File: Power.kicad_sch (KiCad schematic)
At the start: 1 part

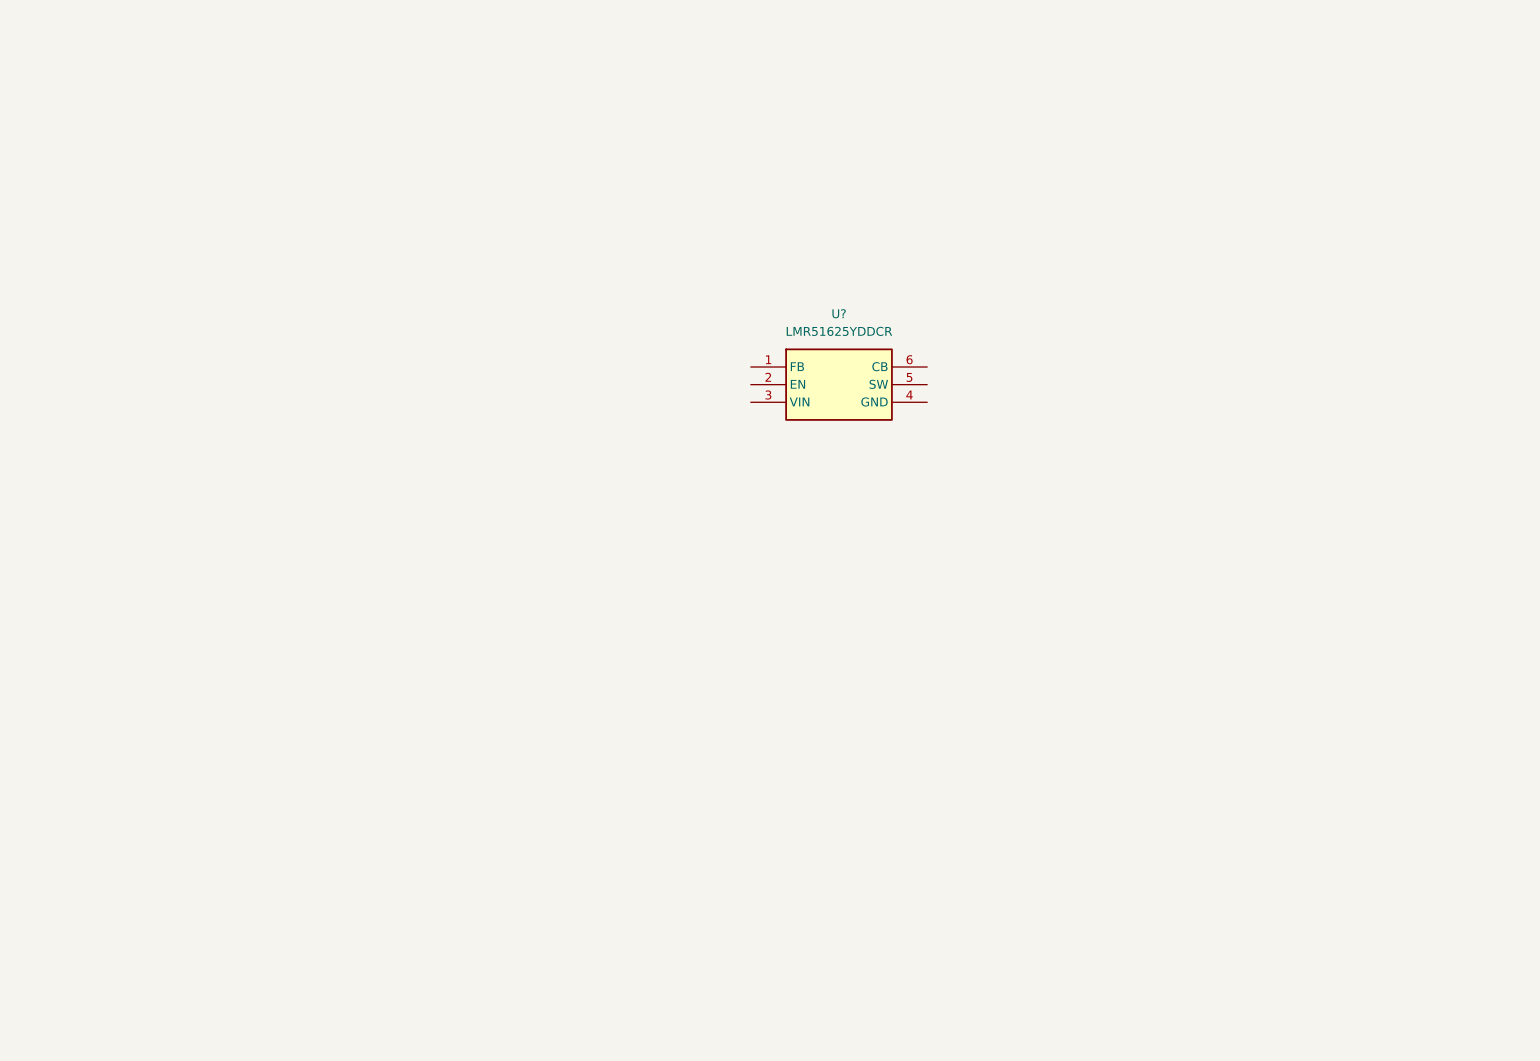
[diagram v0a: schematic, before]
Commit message: add power, some mcu components
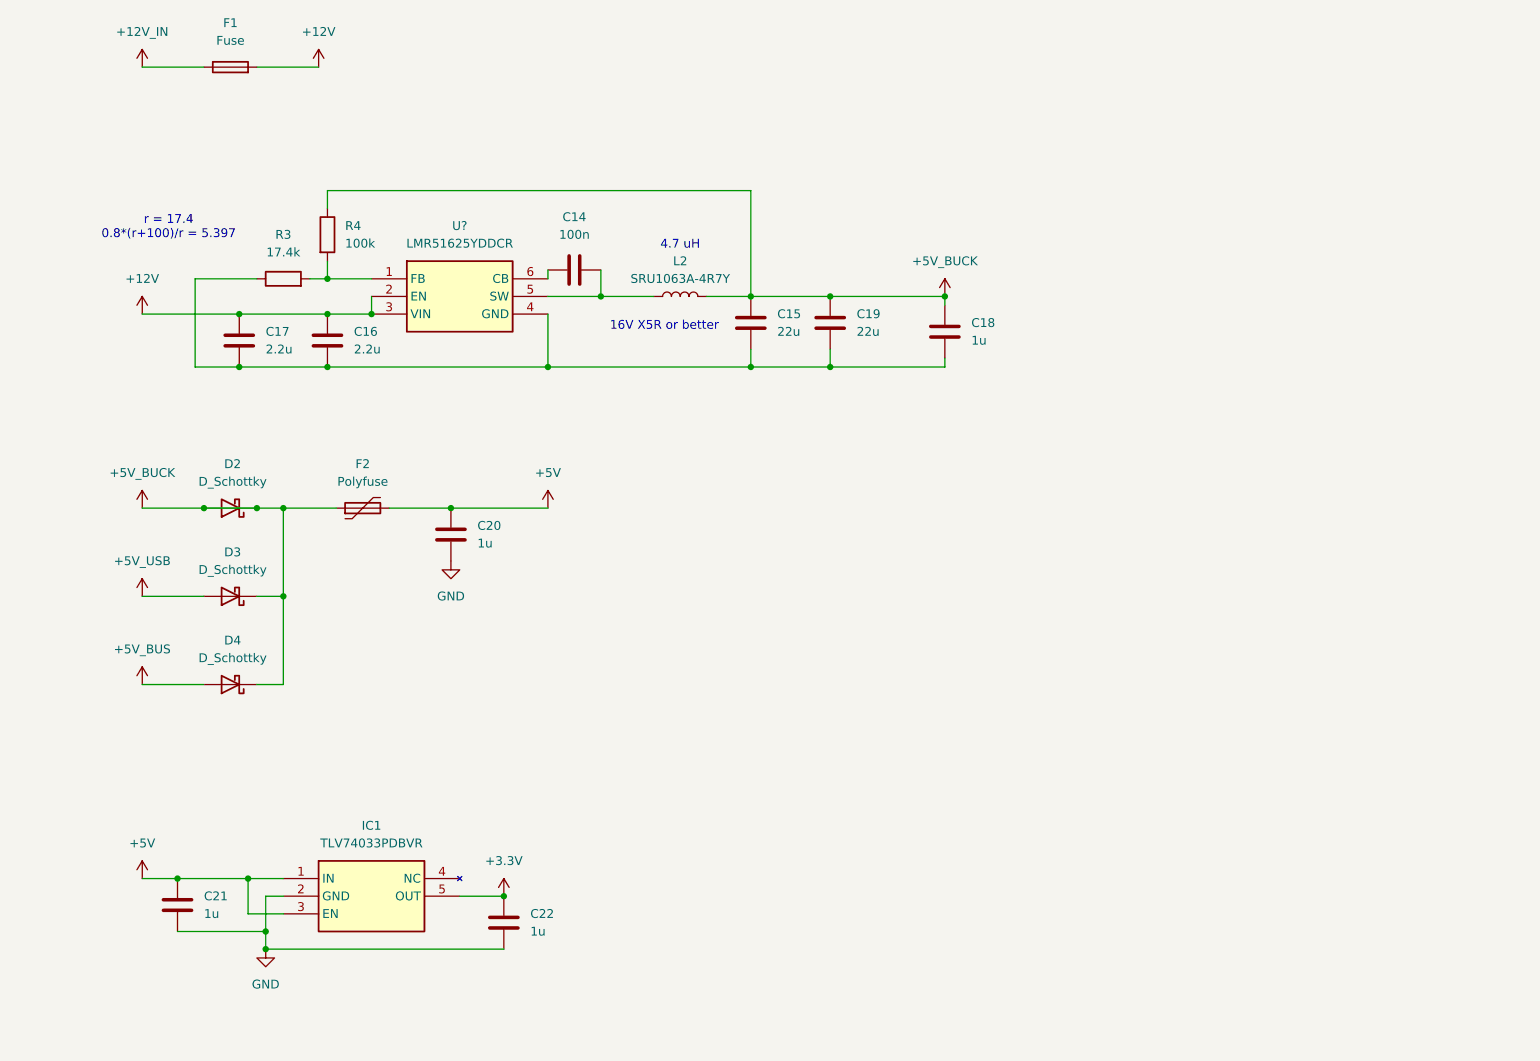
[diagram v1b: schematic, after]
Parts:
- added C14: 100n, Capacitor_SMD:C_0603_1608Metric_Pad1.08x0.95mm_HandSolder, symbol Device:C
- added C15, C19: 22u, Capacitor_SMD:C_1206_3216Metric_Pad1.33x1.80mm_HandSolder, symbol Device:C
- added C16, C17: 2.2u, Capacitor_SMD:C_0603_1608Metric_Pad1.08x0.95mm_HandSolder, symbol Device:C
- added C18, C20, C21, C22: 1u, Capacitor_SMD:C_0603_1608Metric_Pad1.08x0.95mm_HandSolder, symbol Device:C
- added D2, D3, D4: D_Schottky, Diode_SMD:D_SMA_Handsoldering, symbol Device:D_Schottky
- added F1: Fuse, Fuse:Fuseholder_Blade_Mini_Keystone_3568, symbol Device:Fuse
- added F2: Polyfuse, Fuse:Fuse_1812_4532Metric_Pad1.30x3.40mm_HandSolder, symbol Device:Polyfuse
- added IC1: TLV74033PDBVR, SamacSys_Parts:SOT95P280X145-5N, symbol SamacSys_Parts:TLV74033PDBVR
- added L2: SRU1063A-4R7Y, Inductor_SMD:L_Bourns-SRU1028_10.0x10.0mm, symbol Device:L
- added R3: 17.4k, Resistor_SMD:R_0603_1608Metric_Pad0.98x0.95mm_HandSolder, symbol Device:R
- added R4: 100k, Resistor_SMD:R_0603_1608Metric_Pad0.98x0.95mm_HandSolder, symbol Device:R
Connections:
- net at U?.1 (FB): now also R3.2, R4.2
- net +12V: now reaches U?.2 (EN)
- net +12V: now also U?.3 (VIN), C16.1, C17.1, F1.2
- net at U?.4 (GND): now also C15.2, C16.2, C17.2, C18.2, C19.2, R3.1
- net at U?.5 (SW): now also C14.2, L2.1
- net at U?.6 (CB): now also C14.1
- new net +12V_IN: F1.1
- new net +3.3V: C22.1, IC1.5 (OUT)
- new net +5V: C20.1, C21.1, F2.2, IC1.1 (IN), IC1.3 (EN)
- new net +5V_BUCK: C15.1, C18.1, C19.1, D2.1 (K), D2.2 (A), D3.1 (K), D4.1 (K), F2.1, L2.2, R4.1
- new net +5V_BUS: D4.2 (A)
- new net +5V_USB: D3.2 (A)
- new net GND: C20.2, C21.2, C22.2, IC1.2 (GND)
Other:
- note added: "16V X5R or better"
- note added: "4.7 uH"
- note added: "r = 17.4 0.8*(r+100)/r = 5.397"
- moved on the sheet: U?

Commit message: complete schematic, initial board layout
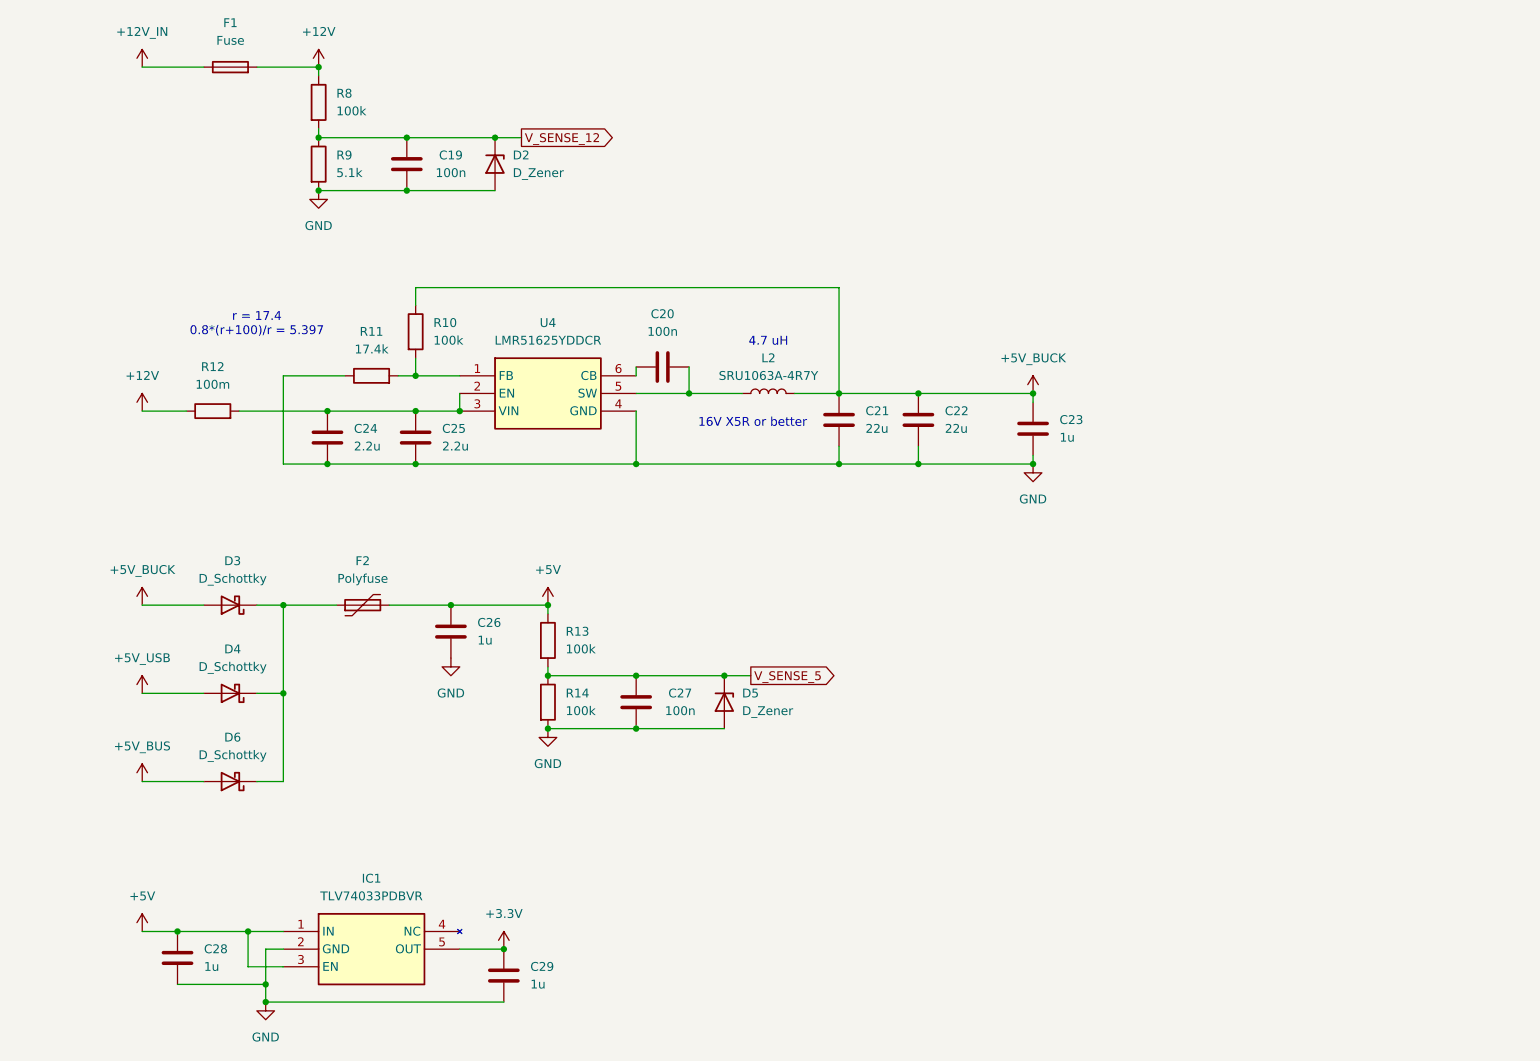
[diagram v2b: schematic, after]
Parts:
- added C19, C27: 100n, Capacitor_SMD:C_0603_1608Metric_Pad1.08x0.95mm_HandSolder, symbol Device:C
- added D2, D5: D_Zener, Diode_SMD:D_SOD-323, symbol Device:D_Zener
- added R12: 100m, Resistor_SMD:R_1206_3216Metric_Pad1.30x1.75mm_HandSolder, symbol Device:R
- added R13, R14, R8: 100k, Resistor_SMD:R_0603_1608Metric_Pad0.98x0.95mm_HandSolder, symbol Device:R
- added R9: 5.1k, Resistor_SMD:R_0603_1608Metric_Pad0.98x0.95mm_HandSolder, symbol Device:R
- D3: renamed from D2; footprint Diode_SMD:D_SMA_Handsoldering -> Diode_SMD:D_SMA
- D4: renamed from D3; footprint Diode_SMD:D_SMA_Handsoldering -> Diode_SMD:D_SMA
- D6: renamed from D4; footprint Diode_SMD:D_SMA_Handsoldering -> Diode_SMD:D_SMA
- gave numbers to parts that had none: 1
- renumbered C14 to C20, C15 to C21, C19 to C22, C18 to C23, C17 to C24, C16 to C25, C20 to C26, C21 to C28, C22 to C29, R4 to R10, R3 to R11
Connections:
- net +12V: now also R12.1, R8.1; no longer C24.1, C25.1, U4.2 (EN), U4.3 (VIN)
- net +5V: now also R13.1
- net +5V_BUCK: no longer D3.1 (K), D4.1 (K), D6.1 (K), F2.1
- net GND: now also C21.2, C22.2, C23.2, C24.2, C25.2, R11.1, U4.4 (GND), C19.2, C27.2, D2.2 (A), D5.2 (A), R14.2, R9.2
- new net: C24.1, C25.1, R12.2, U4.2 (EN), U4.3 (VIN)
- new net: D3.1 (K), D4.1 (K), D6.1 (K), F2.1
- new net V_SENSE_12: C19.1, D2.1 (K), R8.2, R9.1
- new net V_SENSE_5: C27.1, D5.1 (K), R13.2, R14.1
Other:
- moved on the sheet: C20, C21, C22, C23, C24, C25, C26, C28, C29, D3, D4, D6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

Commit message: layout almost complete
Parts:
- D2, D5: footprint Diode_SMD:D_SOD-323 -> Diode_SMD:D_SOD-323_HandSoldering
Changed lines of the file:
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@@
 			)
 		)
-		(property "Footprint" "Diode_SMD:D_SOD-323"
+		(property "Footprint" "Diode_SMD:D_SOD-323_HandSoldering"
 			(at 121.92 124.46 0)
 			(effects
@@
 			)
 		)
-		(property "Footprint" "Diode_SMD:D_SOD-323"
+		(property "Footprint" "Diode_SMD:D_SOD-323_HandSoldering"
 			(at 88.9 46.99 0)
 			(effects

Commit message: completed layout and routing
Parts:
- added D10, D11, D12: LED, LED_SMD:LED_0603_1608Metric_Pad1.05x0.95mm_HandSolder, symbol Device:LED
- added R22, R23, R24: 470, Resistor_SMD:R_0603_1608Metric_Pad0.98x0.95mm_HandSolder, symbol Device:R
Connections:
- net +12V: now also R22.1
- net +3.3V: now also R24.1
- net +5V: now also R23.1
- net GND: now also D10.1 (K), D11.1 (K), D12.1 (K)
- new net: D11.2 (A), R23.2
- new net: D12.2 (A), R24.2
- new net: D10.2 (A), R22.2

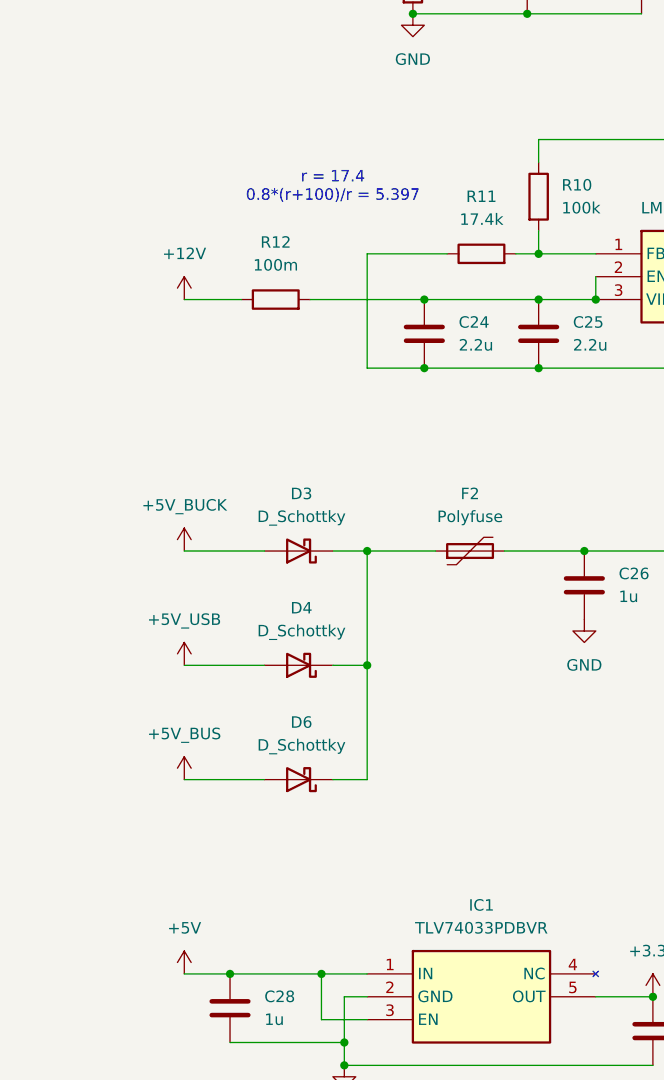
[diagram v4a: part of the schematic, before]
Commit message: adjusted input power section, completed silkscreen text
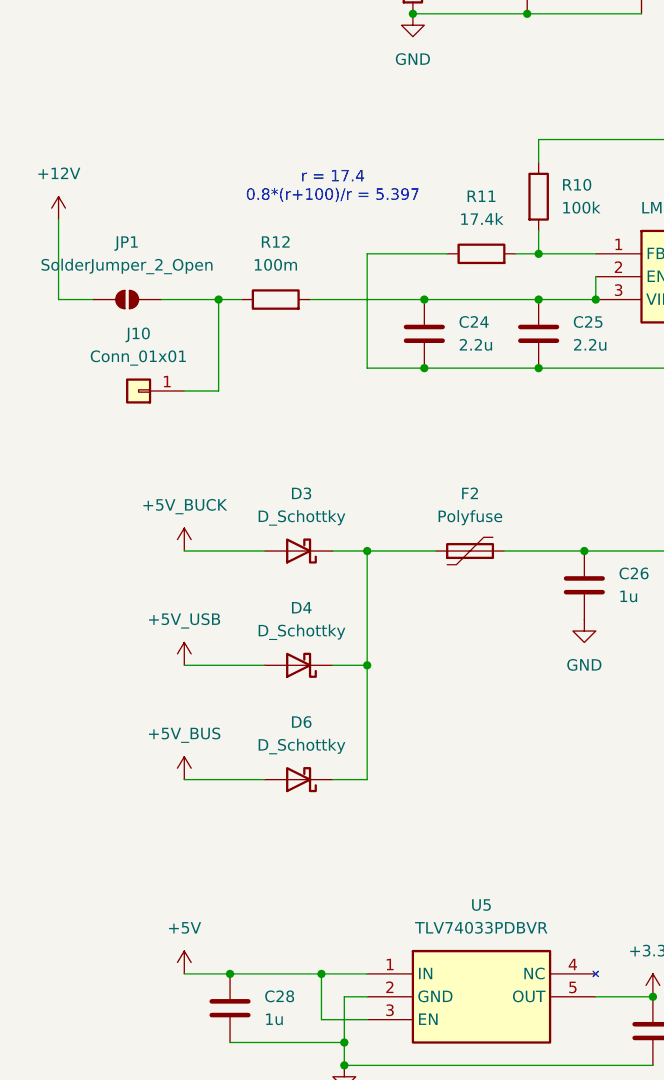
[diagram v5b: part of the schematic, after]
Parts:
- added J10: Conn_01x01, Connector_PinHeader_2.54mm:PinHeader_1x01_P2.54mm_Vertical, symbol Connector_Generic:Conn_01x01
- added JP1: SolderJumper_2_Open, Jumper:SolderJumper-2_P1.3mm_Open_RoundedPad1.0x1.5mm, symbol Jumper:SolderJumper_2_Open
- renumbered IC1 to U5
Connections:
- net +12V: now also JP1.1 (A); no longer R12.1
- new net: J10.1 (Pin_1), JP1.2 (B), R12.1
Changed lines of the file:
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@@
 	)
 	(junction
+		(at 41.91 82.55)
+		(diameter 0)
+		(color 0 0 0 0)
+	)
+	(junction
 		(at 166.37 90.17)
 		(diameter 0)
@@
 	(wire
 		(pts
+			(xy 41.91 82.55) (xy 44.45 82.55)
+		)
+		(stroke
+			(width 0)
+			(type default)
+		)
+	)
+	(wire
+		(pts
 			(xy 43.18 165.1) (xy 55.88 165.1)
 		)
@@
 	(wire
 		(pts
+			(xy 24.13 82.55) (xy 24.13 73.66)
+		)
+		(stroke
+			(width 0)
+			(type default)
+		)
+	)
+	(wire
+		(pts
 			(xy 209.55 81.28) (xy 217.17 81.28)
 		)
@@
 	(wire
 		(pts
+			(xy 35.56 82.55) (xy 41.91 82.55)
+		)
+		(stroke
+			(width 0)
+			(type default)
+		)
+	)
+	(wire
+		(pts
 			(xy 53.34 162.56) (xy 53.34 157.48)
 		)
@@
 	(wire
 		(pts
-			(xy 38.1 82.55) (xy 44.45 82.55)
-		)
-		(stroke
-			(width 0)
-			(type default)
-		)
-	)
-	(wire
-		(pts
 			(xy 88.9 43.18) (xy 92.71 43.18)
 		)
@@
 	(wire
 		(pts
+			(xy 38.1 92.71) (xy 41.91 92.71)
+		)
+		(stroke
+			(width 0)
+			(type default)
+		)
+	)
+	(wire
+		(pts
 			(xy 226.06 81.28) (xy 224.79 81.28)
 		)
@@
 	(wire
 		(pts
+			(xy 41.91 92.71) (xy 41.91 82.55)
+		)
+		(stroke
+			(width 0)
+			(type default)
+		)
+	)
+	(wire
+		(pts
 			(xy 58.42 123.19) (xy 58.42 110.49)
 		)
@@
 	(wire
 		(pts
+			(xy 27.94 82.55) (xy 24.13 82.55)
+		)
+		(stroke
+			(width 0)
+			(type default)
+		)
+	)
+	(wire
+		(pts
 			(xy 63.5 43.18) (xy 63.5 41.91)
 		)
@@
 	)
 	(symbol
+		(lib_id "Jumper:SolderJumper_2_Open")
+		(at 31.75 82.55 0)
+		(unit 1)
+		(exclude_from_sim no)
+		(in_bom no)
+		(on_board yes)
+		(dnp no)
+		(fields_autoplaced yes)
+		(property "Reference" "JP1"
+			(at 31.75 76.2 0)
+			(effects
+				(font
+					(size 1.27 1.27)
+				)
+			)
+		)
+		(property "Value" "SolderJumper_2_Open"
+			(at 31.75 78.74 0)
+			(effects
+				(font
+					(size 1.27 1.27)
+				)
+			)
+		)
+		(property "Footprint" "Jumper:SolderJumper-2_P1.3mm_Open_RoundedPad1.0x1.5mm"
+			(at 31.75 82.55 0)
+			(effects
+				(font
+					(size 1.27 1.27)
+				)
+				(hide yes)
+			)
+		)
+		(property "Datasheet" "~"
+			(at 31.75 82.55 0)
+			(effects
+				(font
+					(size 1.27 1.27)
+				)
+				(hide yes)
+			)
+		)
+		(property "Description" "Solder Jumper, 2-pole, open"
+			(at 31.75 82.55 0)
+			(effects
+				(font
+					(size 1.27 1.27)
+				)
+				(hide yes)
+			)
+		)
+		(pin "2"
+		)
+		(pin "1"
+		)
+		(instances
+			(project ""
+				(path "/f2bb7816-6b2a-47fd-8906-eb4aedd6f9e6/5e700bbe-1f69-4433-b621-e458f2a62014"
+					(reference "JP1")
+					(unit 1)
+				)
+			)
+		)
+	)
+	(symbol
 		(lib_id "Device:R")
 		(at 63.5 38.1 0)
@@
 	(symbol
 		(lib_id "power:+3.3V")
-		(at 38.1 82.55 0)
+		(at 24.13 73.66 0)
 		(unit 1)
 		(exclude_from_sim no)
@@
 		(fields_autoplaced yes)
 		(property "Reference" "#PWR034"
-			(at 38.1 86.36 0)
+			(at 24.13 77.47 0)
 			(effects
 				(font
@@
 		)
 		(property "Value" "+12V"
-			(at 38.1 77.47 0)
+			(at 24.13 68.58 0)
 			(effects
 				(font
@@
 		)
 		(property "Footprint" ""
-			(at 38.1 82.55 0)
+			(at 24.13 73.66 0)
 			(effects
 				(font
@@
 		)
 		(property "Datasheet" ""
-			(at 38.1 82.55 0)
+			(at 24.13 73.66 0)
 			(effects
 				(font
@@
 		)
 		(property "Description" "Power symbol creates a global label with name \"+3.3V\""
-			(at 38.1 82.55 0)
+			(at 24.13 73.66 0)
 			(effects
 				(font
@@
 		(dnp no)
 		(fields_autoplaced yes)
-		(property "Reference" "IC1"
+		(property "Reference" "U5"
 			(at 71.12 149.86 0)
 			(effects
@@
 			(project ""
 				(path "/f2bb7816-6b2a-47fd-8906-eb4aedd6f9e6/5e700bbe-1f69-4433-b621-e458f2a62014"
-					(reference "IC1")
+					(reference "U5")
 					(unit 1)
 				)
@@
 					(unit 1)
 				)
+			)
+		)
+	)
+	(symbol
+		(lib_id "Connector_Generic:Conn_01x01")
+		(at 33.02 92.71 180)
+		(unit 1)
+		(exclude_from_sim no)
+		(in_bom yes)
+		(on_board yes)
+		(dnp no)
+		(fields_autoplaced yes)
+		(property "Reference" "J10"
+			(at 33.02 86.36 0)
+			(effects
+				(font
+					(size 1.27 1.27)
+				)
+			)
+		)
+		(property "Value" "Conn_01x01"
+			(at 33.02 88.9 0)
+			(effects
+				(font
+					(size 1.27 1.27)
+				)
+			)
+		)
+		(property "Footprint" "Connector_PinHeader_2.54mm:PinHeader_1x01_P2.54mm_Vertical"
+			(at 33.02 92.71 0)
+			(effects
+				(font
+					(size 1.27 1.27)
+				)
+				(hide yes)
+			)
+		)
+		(property "Datasheet" "~"
+			(at 33.02 92.71 0)
+			(effects
+				(font
+					(size 1.27 1.27)
+				)
+				(hide yes)
+			)
+		)
+		(property "Description" "Generic connector, single row, 01x01, script generated (kicad-library-utils/schlib/autogen/connector/)"
+			(at 33.02 92.71 0)
+			(effects
+				(font
+					(size 1.27 1.27)
+				)
+				(hide yes)
+			)
+		)
+		(pin "1"
+		)
+		(instances
+			(project "LV3-Core"
+				(path "/f2bb7816-6b2a-47fd-8906-eb4aedd6f9e6/5e700bbe-1f69-4433-b621-e458f2a62014"
+					(reference "J10")
+					(unit 1)
+				)

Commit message: minor silkscreen changes, add reverse block diode for 12v ORDER 23 october 2025
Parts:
- added D13: D_Schottky, Diode_SMD:D_SOD-123F, symbol Device:D_Schottky
- R22: value 470 -> 2.2k
- R24: value 470 -> 120
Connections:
- net at J10.1 (Pin_1), JP1.2 (B): now also D13.2 (A); no longer R12.1
- new net: D13.1 (K), R12.1
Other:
- moved on the sheet: C20, C21, C22, C23, C24, C25, L2, R10, R11, R12, U4
